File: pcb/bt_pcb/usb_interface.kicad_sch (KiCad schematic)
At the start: 6 parts, among them J12 USB_C_Receptacle

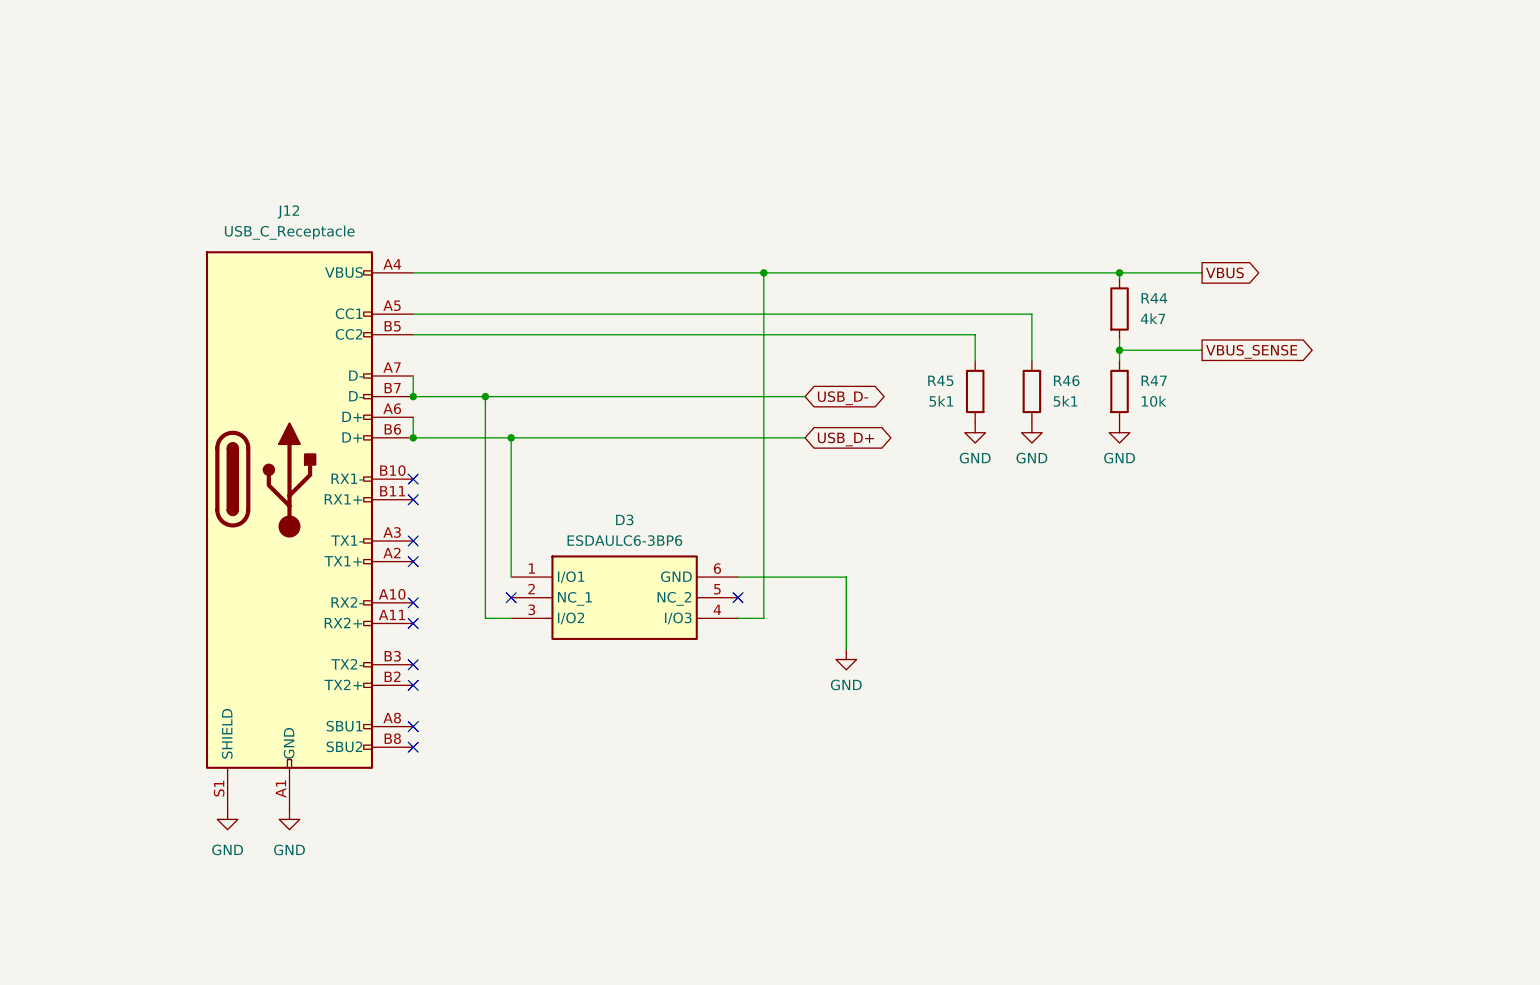
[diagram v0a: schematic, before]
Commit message: ditching power pcb, new codec
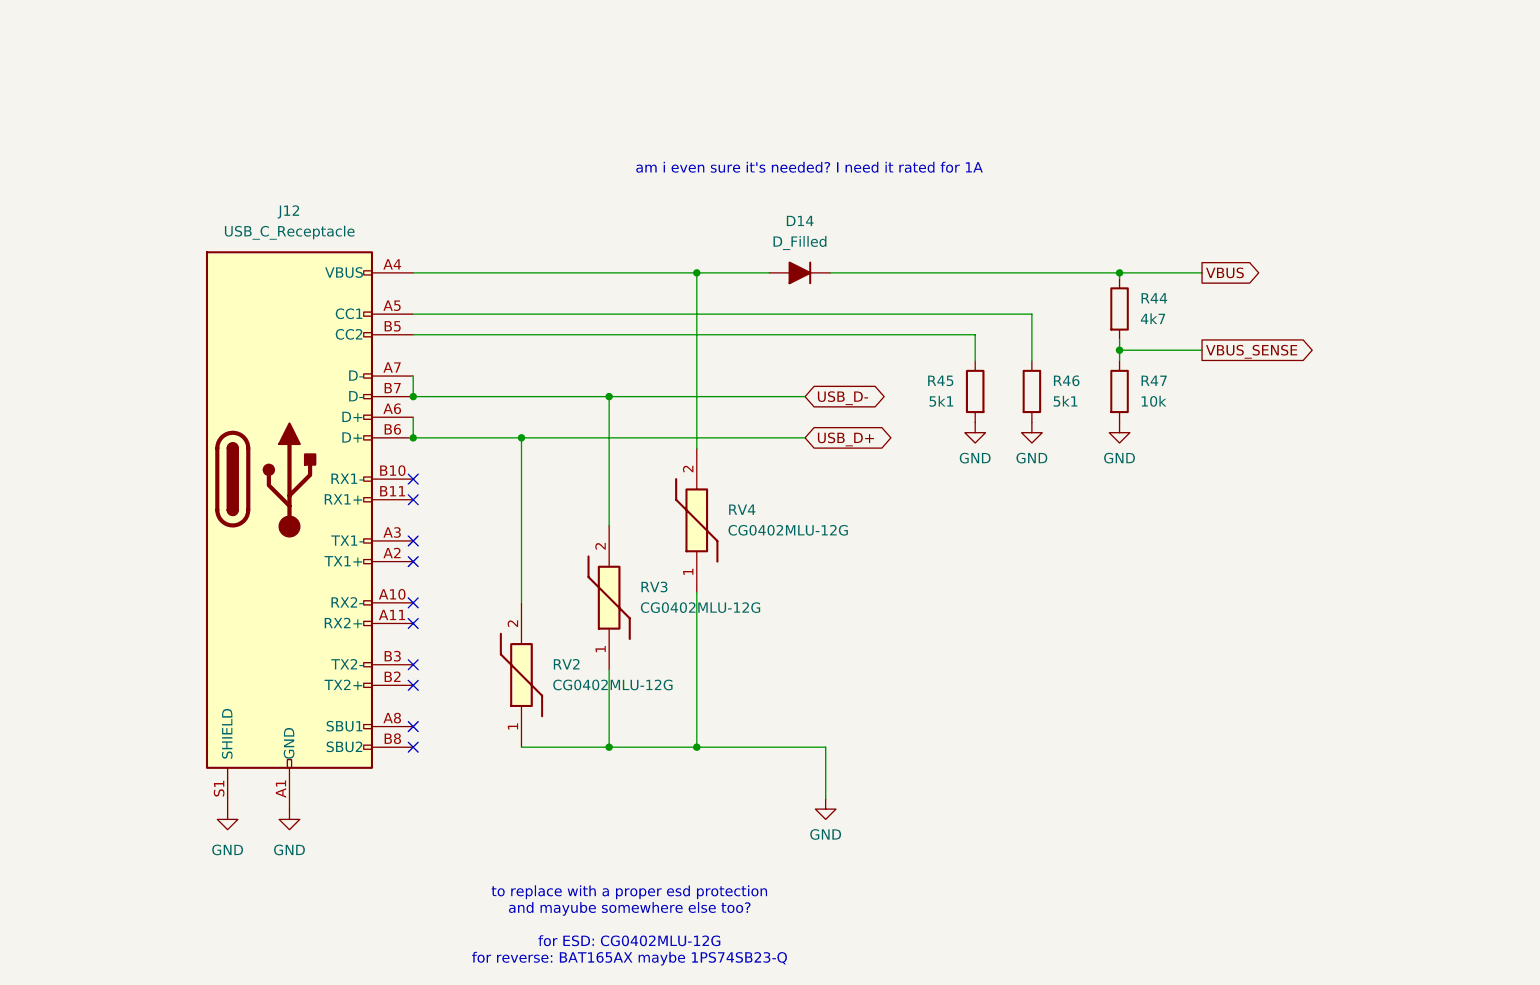
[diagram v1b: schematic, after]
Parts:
- removed D3: ESDAULC6-3BP6, library:ESDAULC63BP6, symbol library:ESDAULC6-3BP6
- added D14: D_Filled, symbol Device:D_Filled
- added RV2, RV3, RV4: CG0402MLU-12G, VARC1005X41N, symbol library:CG0402MLU-12G
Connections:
- net GND: now also RV2.1, RV3.1, RV4.1
- net USB_D+: now also RV2.2
- net USB_D-: now also RV3.2
- net VBUS: now also D14.1 (K); no longer J12.A4 (VBUS), J12.A9 (VBUS), J12.B4 (VBUS), J12.B9 (VBUS)
- new net: D14.2 (A), J12.A4 (VBUS), J12.A9 (VBUS), J12.B4 (VBUS), J12.B9 (VBUS), RV4.2
- no-connect marks 12 -> 10
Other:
- note added: "am i even sure it's needed? I need it rated for 1A"
- note added: "to replace with a proper esd protection and mayube somewhere else too? for ESD: CG0402MLU-12G for reverse: BAT165AX maybe 1PS74SB23-Q"

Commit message: complete makeover of power supply
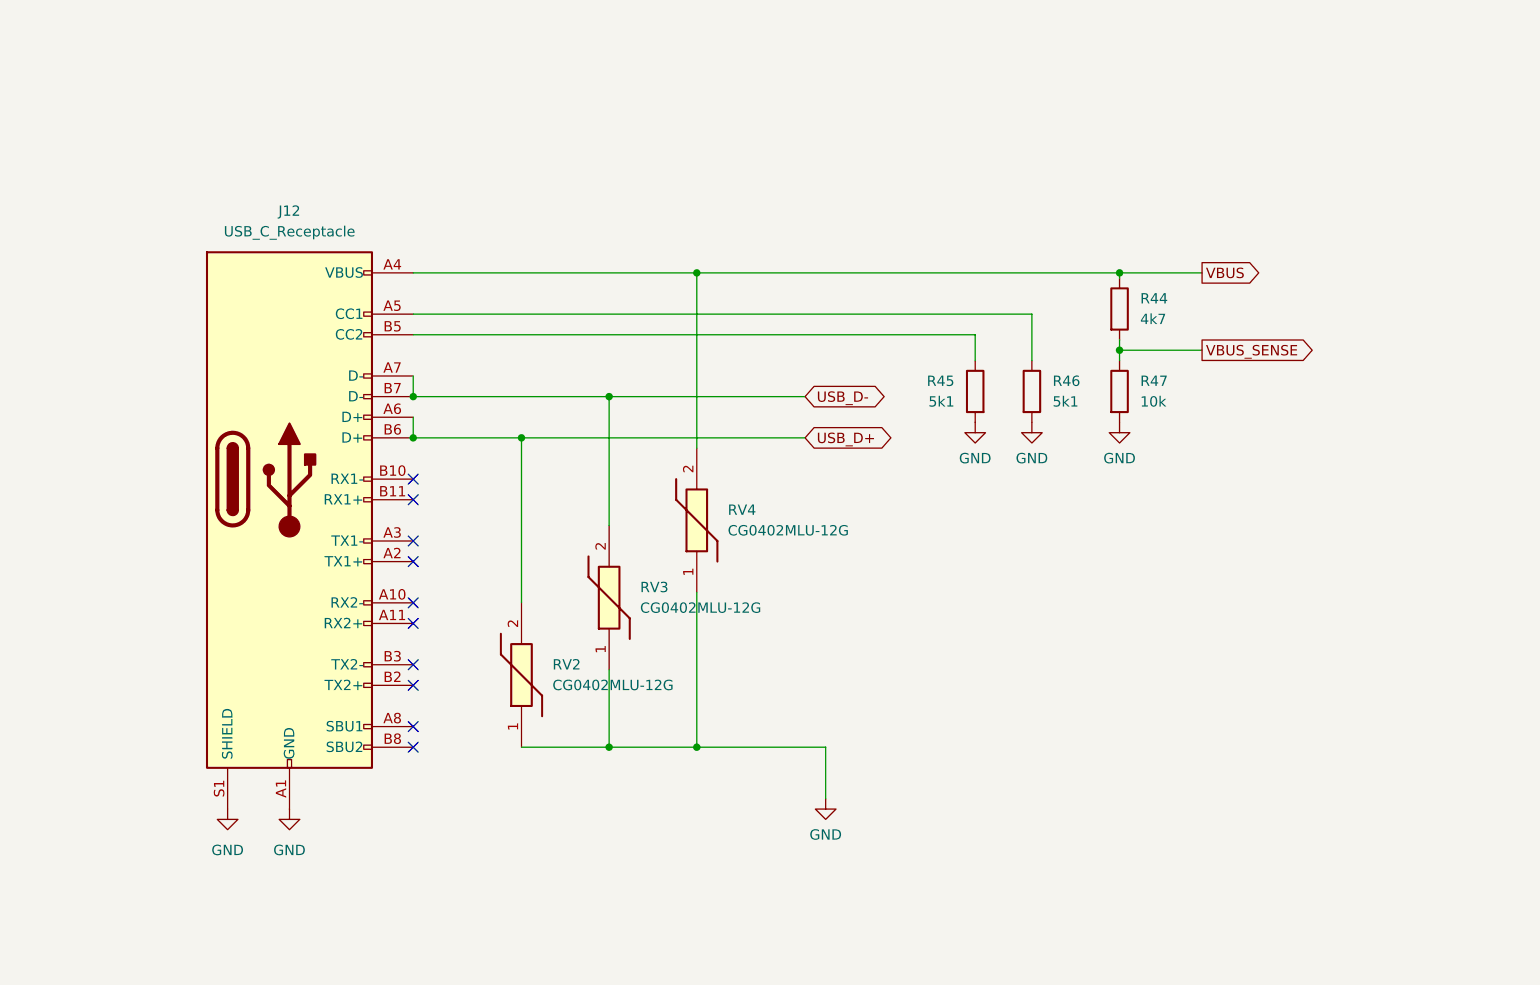
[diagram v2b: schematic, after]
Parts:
- removed D14: D_Filled, symbol Device:D_Filled
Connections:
- net VBUS: now also J12.A4 (VBUS), J12.A9 (VBUS), J12.B4 (VBUS), J12.B9 (VBUS), RV4.2
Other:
- note removed: "am i even sure it's needed? I need it rated for 1A"
- note removed: "to replace with a proper esd protection and mayube somewhere else too? for ESD: CG0402MLU-12G for reverse: BAT165AX maybe 1PS74SB23-Q"
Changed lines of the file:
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@@
 	(generator_version "9.0")
 	(paper "A4")
-	(text "am i even sure it's needed? I need it rated for 1A\n"
-		(exclude_from_sim no)
-		(at 169.418 63.5 0)
-		(effects
-			(font
-				(size 1.27 1.27)
-			)
-		)
-	)
-	(text "to replace with a proper esd protection\nand mayube somewhere else too?\n\nfor ESD: CG0402MLU-12G\nfor reverse: BAT165AX maybe 1PS74SB23-Q"
-		(exclude_from_sim no)
-		(at 147.32 156.718 0)
-		(effects
-			(font
-				(size 1.27 1.27)
-			)
-		)
-	)
 	(junction
 		(at 133.985 96.52)
@@
 	(wire
 		(pts
-			(xy 172.085 76.2) (xy 207.645 76.2)
-		)
-		(stroke
-			(width 0)
-			(type default)
-		)
-	)
-	(wire
-		(pts
 			(xy 120.65 76.2) (xy 155.575 76.2)
 		)
@@
 	(wire
 		(pts
-			(xy 155.575 76.2) (xy 164.465 76.2)
+			(xy 155.575 76.2) (xy 207.645 76.2)
 		)
 		(stroke
@@
 					(unit 1)
 				)
-			)
-		)
-	)
-	(symbol
-		(lib_id "Device:D_Filled")
-		(at 168.275 76.2 180)
-		(unit 1)
-		(exclude_from_sim no)
-		(in_bom yes)
-		(on_board yes)
-		(dnp no)
-		(fields_autoplaced yes)
-		(property "Reference" "D14"
-			(at 168.275 69.85 0)
-			(effects
-				(font
-					(size 1.27 1.27)
-				)
-			)
-		)
-		(property "Value" "D_Filled"
-			(at 168.275 72.39 0)
-			(effects
-				(font
-					(size 1.27 1.27)
-				)
-			)
-		)
-		(property "Footprint" ""
-			(at 168.275 76.2 0)
-			(effects
-				(font
-					(size 1.27 1.27)
-				)
-				(hide yes)
-			)
-		)
-		(property "Datasheet" "~"
-			(at 168.275 76.2 0)
-			(effects
-				(font
-					(size 1.27 1.27)
-				)
-				(hide yes)
-			)
-		)
-		(property "Description" "Diode, filled shape"
-			(at 168.275 76.2 0)
-			(effects
-				(font
-					(size 1.27 1.27)
-				)
-				(hide yes)
-			)
-		)
-		(property "Sim.Device" "D"
-			(at 168.275 76.2 0)
-			(effects
-				(font
-					(size 1.27 1.27)
-				)
-				(hide yes)
-			)
-		)
-		(property "Sim.Pins" "1=K 2=A"
-			(at 168.275 76.2 0)
-			(effects
-				(font
-					(size 1.27 1.27)
-				)
-				(hide yes)
-			)
-		)
-		(pin "1"
-		)
-		(pin "2"
-		)
-		(instances
-			(project "bt_pcb"
-				(path "/eb787481-08cd-41a4-a128-173fa6227c32/81f44120-5006-4955-ab2c-f15dbf34b899"
-					(reference "D14")
-					(unit 1)
-				)

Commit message: big progress, now revising error and warnings
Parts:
- RV2, RV3, RV4: footprint VARC1005X41N -> library:VARC1005X41N

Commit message: solving some erc warnings and errors
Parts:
- renumbered J12 to J4, R45 to R3, R46 to R4, R44 to R5, R47 to R6, RV2 to RV1, RV3 to RV2, RV4 to RV3
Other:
- moved on the sheet: R3, R4, R5, R6, RV1, RV2, RV3

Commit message: schematic in theory finished
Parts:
- J5: renamed from J4; footprint (none) -> library:UJ32CHGSMTTR68
- R10: renamed from R6; footprint (none) -> Resistor_SMD:R_0603_1608Metric_Pad0.98x0.95mm_HandSolder
- R7: renamed from R5; footprint (none) -> Resistor_SMD:R_0603_1608Metric_Pad0.98x0.95mm_HandSolder
- R8: renamed from R3; footprint (none) -> Resistor_SMD:R_0603_1608Metric_Pad0.98x0.95mm_HandSolder
- R9: renamed from R4; footprint (none) -> Resistor_SMD:R_0603_1608Metric_Pad0.98x0.95mm_HandSolder
- renumbered RV3 to RV1, RV1 to RV3
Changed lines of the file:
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@@
 		(dnp no)
 		(fields_autoplaced yes)
-		(property "Reference" "RV1"
+		(property "Reference" "RV3"
 			(at 138.43 124.4599 90)
 			(effects
@@
 			(project ""
 				(path "/eb787481-08cd-41a4-a128-173fa6227c32/81f44120-5006-4955-ab2c-f15dbf34b899"
-					(reference "RV1")
+					(reference "RV3")
 					(unit 1)
 				)
@@
 		(dnp no)
 		(fields_autoplaced yes)
-		(property "Reference" "#PWR026"
+		(property "Reference" "#PWR027"
 			(at 156.21 140.97 0)
 			(effects
@@
 			(project "bt_pcb"
 				(path "/eb787481-08cd-41a4-a128-173fa6227c32/81f44120-5006-4955-ab2c-f15dbf34b899"
-					(reference "#PWR026")
+					(reference "#PWR027")
 					(unit 1)
 				)
@@
 		(dnp no)
 		(fields_autoplaced yes)
-		(property "Reference" "J4"
+		(property "Reference" "J5"
 			(at 105.41 68.58 0)
 			(effects
@@
 			)
 		)
-		(property "Footprint" ""
+		(property "Footprint" "library:UJ32CHGSMTTR68"
 			(at 109.22 101.6 0)
 			(effects
@@
 			(project "bt_pcb"
 				(path "/eb787481-08cd-41a4-a128-173fa6227c32/81f44120-5006-4955-ab2c-f15dbf34b899"
-					(reference "J4")
+					(reference "J5")
 					(unit 1)
 				)
@@
 		(dnp no)
 		(fields_autoplaced yes)
-		(property "Reference" "R4"
+		(property "Reference" "R9"
 			(at 199.39 90.17 0)
 			(effects
@@
 			)
 		)
-		(property "Footprint" ""
+		(property "Footprint" "Resistor_SMD:R_0603_1608Metric_Pad0.98x0.95mm_HandSolder"
 			(at 195.072 91.44 90)
 			(effects
@@
 			(project "bt_pcb"
 				(path "/eb787481-08cd-41a4-a128-173fa6227c32/81f44120-5006-4955-ab2c-f15dbf34b899"
-					(reference "R4")
+					(reference "R9")
 					(unit 1)
 				)
@@
 		(dnp no)
 		(fields_autoplaced yes)
-		(property "Reference" "#PWR029"
+		(property "Reference" "#PWR026"
 			(at 208.28 101.6 0)
 			(effects
@@
 			(project "bt_pcb"
 				(path "/eb787481-08cd-41a4-a128-173fa6227c32/81f44120-5006-4955-ab2c-f15dbf34b899"
-					(reference "#PWR029")
+					(reference "#PWR026")
 					(unit 1)
 				)
@@
 		(dnp no)
 		(fields_autoplaced yes)
-		(property "Reference" "#PWR028"
+		(property "Reference" "#PWR025"
 			(at 196.85 101.6 0)
 			(effects
@@
 			(project "bt_pcb"
 				(path "/eb787481-08cd-41a4-a128-173fa6227c32/81f44120-5006-4955-ab2c-f15dbf34b899"
-					(reference "#PWR028")
+					(reference "#PWR025")
 					(unit 1)
 				)
@@
 		(on_board yes)
 		(dnp no)
-		(property "Reference" "R3"
+		(property "Reference" "R8"
 			(at 187.96 90.17 0)
 			(effects
@@
 			)
 		)
-		(property "Footprint" ""
+		(property "Footprint" "Resistor_SMD:R_0603_1608Metric_Pad0.98x0.95mm_HandSolder"
 			(at 192.278 91.44 90)
 			(effects
@@
 			(project "bt_pcb"
 				(path "/eb787481-08cd-41a4-a128-173fa6227c32/81f44120-5006-4955-ab2c-f15dbf34b899"
-					(reference "R3")
+					(reference "R8")
 					(unit 1)
 				)
@@
 		(dnp no)
 		(fields_autoplaced yes)
-		(property "Reference" "R5"
+		(property "Reference" "R7"
 			(at 210.82 80.01 0)
 			(effects
@@
 			)
 		)
-		(property "Footprint" ""
+		(property "Footprint" "Resistor_SMD:R_0603_1608Metric_Pad0.98x0.95mm_HandSolder"
 			(at 206.502 81.28 90)
 			(effects
@@
 			(project "bt_pcb"
 				(path "/eb787481-08cd-41a4-a128-173fa6227c32/81f44120-5006-4955-ab2c-f15dbf34b899"
-					(reference "R5")
+					(reference "R7")
 					(unit 1)
 				)
@@
 		(dnp no)
 		(fields_autoplaced yes)
-		(property "Reference" "#PWR024"
+		(property "Reference" "#PWR028"
 			(at 97.79 148.59 0)
 			(effects
@@
 			(project ""
 				(path "/eb787481-08cd-41a4-a128-173fa6227c32/81f44120-5006-4955-ab2c-f15dbf34b899"
-					(reference "#PWR024")
+					(reference "#PWR028")
 					(unit 1)
 				)
@@
 		(dnp no)
 		(fields_autoplaced yes)
-		(property "Reference" "R6"
+		(property "Reference" "R10"
 			(at 210.82 90.17 0)
 			(effects
@@
 			)
 		)
-		(property "Footprint" ""
+		(property "Footprint" "Resistor_SMD:R_0603_1608Metric_Pad0.98x0.95mm_HandSolder"
 			(at 206.502 91.44 90)
 			(effects
@@
 			(project "bt_pcb"
 				(path "/eb787481-08cd-41a4-a128-173fa6227c32/81f44120-5006-4955-ab2c-f15dbf34b899"
-					(reference "R6")
+					(reference "R10")
 					(unit 1)
 				)
@@
 		(dnp no)
 		(fields_autoplaced yes)
-		(property "Reference" "RV3"
+		(property "Reference" "RV1"
 			(at 160.02 105.4099 90)
 			(effects
@@
 			(project "bt_pcb"
 				(path "/eb787481-08cd-41a4-a128-173fa6227c32/81f44120-5006-4955-ab2c-f15dbf34b899"
-					(reference "RV3")
+					(reference "RV1")
 					(unit 1)
 				)
@@
 		(dnp no)
 		(fields_autoplaced yes)
-		(property "Reference" "#PWR025"
+		(property "Reference" "#PWR029"
 			(at 105.41 148.59 0)
 			(effects
@@
 			(project "bt_pcb"
 				(path "/eb787481-08cd-41a4-a128-173fa6227c32/81f44120-5006-4955-ab2c-f15dbf34b899"
-					(reference "#PWR025")
+					(reference "#PWR029")
 					(unit 1)
 				)
@@
 		(dnp no)
 		(fields_autoplaced yes)
-		(property "Reference" "#PWR027"
+		(property "Reference" "#PWR024"
 			(at 190.5 101.6 0)
 			(effects
@@
 			(project "bt_pcb"
 				(path "/eb787481-08cd-41a4-a128-173fa6227c32/81f44120-5006-4955-ab2c-f15dbf34b899"
-					(reference "#PWR027")
-					(unit 1)
-				)
+					(reference "#PWR024")
+					(unit 1)
+				)

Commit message: pcb started
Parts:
- removed J5: USB_C_Receptacle, library:UJ32CHGSMTTR68, symbol Connector:USB_C_Receptacle
- removed R8, R9: 5k1, Resistor_SMD:R_0603_1608Metric_Pad0.98x0.95mm_HandSolder, symbol Device:R
- added J6: UJ32-C-H-G-SMT-TR-68, library:UJ32CHGSMTTR68, symbol library:UJ32-C-H-G-SMT-TR-68
- added R10, R11: 5k1, Resistor_SMD:R_0603_1608Metric_Pad0.98x0.95mm_HandSolder, symbol Device:R
- renumbered R7 to R8, R10 to R9
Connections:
- net GND: now also J6.A1 (GND_1), J6.A12 (GND_2), J6.B1 (GND_3), J6.B12 (GND_4), J6.MH3, J6.MH4, J6.MH5, J6.MH6, R10.2, R11.2
- net USB_D+: now also J6.A7 (DN1), J6.B7 (DN2)
- net USB_D-: now also J6.A6 (DP1), J6.B6 (DP2)
- net VBUS: now also J6.A4 (VBUS_1), J6.A9 (VBUS_2), J6.B4 (VBUS_3), J6.B9 (VBUS_4)
- new net: J6.A5 (CC1), R11.1
- new net: J6.B5 (CC2), R10.1
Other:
- moved on the sheet: R8, R9, RV1, RV2, RV3
